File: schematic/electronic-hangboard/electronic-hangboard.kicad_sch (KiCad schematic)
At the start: 40 parts, among them J1 UART, J2 Load cell, J3 JTAG, J4 Battery, Q1 2N7002, SW1 RESET, SW2 POWER_ON, U1 ESP32-WROOM-32, U2 HX711, U3 NCP1400A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

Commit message: Update pcb
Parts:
- removed C10: 68uF, Capacitor_SMD:C_1206_3216Metric_Pad1.33x1.80mm_HandSolder, symbol Device:C
- removed C9: 10uF, Capacitor_SMD:C_1206_3216Metric_Pad1.33x1.80mm_HandSolder, symbol Device:C
- removed D1: MBR0520LT1, Diode_SMD:D_SOD-123, symbol Device:D
- removed J1: UART, Connector_PinHeader_2.54mm:PinHeader_1x03_P2.54mm_Vertical, symbol Connector_Generic:Conn_01x03
- removed J2: Load cell, Connector_Wire:SolderWire-0.1sqmm_1x04_P3.6mm_D0.4mm_OD1mm_Relief, symbol Connector_Generic:Conn_01x04
- removed J3: JTAG, Connector_PinHeader_2.54mm:PinHeader_1x07_P2.54mm_Vertical, symbol Connector:AVR-JTAG-10
- removed J4: Battery, Connector_Wire:SolderWire-0.1sqmm_1x02_P3.6mm_D0.4mm_OD1mm, symbol Connector_Generic:Conn_01x02
- removed L1: CR54−220MC - 22uH, Inductor_SMD:L_Bourns_SRP7028A_7.3x6.6mm, symbol Device:L
- removed Q1: 2N7002, Package_TO_SOT_SMD:SOT-23, symbol Transistor_FET:2N7002
- removed R8: 100R, Resistor_SMD:R_1206_3216Metric_Pad1.30x1.75mm_HandSolder, symbol Device:R
- removed SW1: RESET, Button_Switch_SMD:SW_Push_1P1T_NO_6x6mm_H9.5mm, symbol Switch:SW_SPST
- removed SW2: POWER_ON, Button_Switch_SMD:SW_Push_1P1T_NO_6x6mm_H9.5mm, symbol Switch:SW_SPST
- removed U3: NCP1400A, Package_TO_SOT_SMD:SOT-23-5_HandSoldering, symbol ncp1400a:NCP1400A
- added C13, C15: 4.7uF, Capacitor_SMD:C_1206_3216Metric_Pad1.33x1.80mm_HandSolder, symbol Device:C
- added C14: 3.3pF, Capacitor_SMD:C_1206_3216Metric_Pad1.33x1.80mm_HandSolder, symbol Device:C
- added D1, D3: LED, Diode_SMD:D_1206_3216Metric_Pad1.42x1.75mm_HandSolder, symbol Device:LED
- added D2: MBR0520LT1, Diode_SMD:D_SOD-123, symbol Device:D
- added J1: BATTERY, Connector_PinHeader_2.54mm:PinHeader_1x02_P2.54mm_Vertical, symbol Connector:Conn_01x02_Pin
- added J2: Conn_01x04_Pin, Connector_PinHeader_2.54mm:PinHeader_1x04_P2.54mm_Vertical, symbol Connector:Conn_01x04_Pin
- added J3: JTAG, Connector_PinHeader_2.54mm:PinHeader_1x06_P2.54mm_Vertical, symbol Connector:Conn_01x06_Pin
- added J4, J6: Conn_01x10_Pin, Connector_PinHeader_2.54mm:PinHeader_1x10_P2.54mm_Vertical, symbol Connector:Conn_01x10_Pin
- added J5: UART, Connector_PinHeader_2.54mm:PinHeader_1x06_P2.54mm_Vertical, symbol Connector:Conn_01x06_Pin
- added L2: 10uH, Inductor_SMD:L_Bourns_SRP7028A_7.3x6.6mm, symbol Device:L
- added Q1: S9015, Package_TO_SOT_SMD:SOT-23, symbol Simulation_SPICE:PNP
- added R1: 620K, Resistor_SMD:R_1206_3216Metric_Pad1.30x1.75mm_HandSolder, symbol Device:R
- added R1: 200K, Resistor_SMD:R_1206_3216Metric_Pad1.30x1.75mm_HandSolder, symbol Device:R
- added R12, R15: 330R, Resistor_SMD:R_1206_3216Metric_Pad1.30x1.75mm_HandSolder, symbol Device:R
- added SW3: POWER_ON, Connector_PinHeader_2.54mm:PinHeader_1x02_P2.54mm_Vertical_SMD_Pin1Left, symbol Switch:SW_SPST
- added U5: TPS61040DBV, Package_TO_SOT_SMD:SOT-23-5, symbol Regulator_Switching:TPS61040DBV
- H1, H2, H3: footprint MountingHole:MountingHole_3.2mm_M3 -> MountingHole:MountingHole_3.2mm_M3_DIN965_Pad_TopBottom
- R1: value R -> 10K
- R9: value 100R -> 1K2
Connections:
- net +3V3: now also J3.1 (Pin_1), J5.1 (Pin_1), Q1.3 (E)
- net +5V: now also C14.2, C15.2, D2.1 (K), R1.1
- net +BATT: now also C13.2, J1.2 (Pin_2), L2.1, SW3.2 (B), U5.5 (VIN)
- net CONV_EN: now also SW3.1 (A), U5.4 (EN)
- net EN: now also J5.4 (Pin_4)
- net GND: now also C13.1, C15.1, J1.1 (Pin_1), J2.2 (Pin_2), J3.2 (Pin_2), J5.2 (Pin_2), R1.2, R12.1, R15.2, U5.2 (GND)
- net RX: now also J5.6 (Pin_6)
- net S+: now also J2.3 (Pin_3)
- net S-: now also C7.2, U2.7 (INA-), J2.4 (Pin_4)
- net SCK: now also U1.20 (SCK/CLK), J4.4 (Pin_4); no longer U1.31 (IO19), U2.11 (PD_SCK)
- net TX: now also J5.5 (Pin_5)
- net at R2.1: now also J3.3 (Pin_3)
- net at R3.1: now also J3.4 (Pin_4)
- net at R4.1: now also J3.5 (Pin_5)
- net at R5.1: now also J3.6 (Pin_6)
- net RST: now reaches U1.25 (IO0)
- net RST: now also J5.3 (Pin_3)
- net E+: now reaches C6.2, R6.1, U2.3 (AVDD)
- net E+: now also J2.1 (Pin_1), Q1.1 (C)
- net at U2.2 (BASE): now also Q1.2 (B)
- net IO25: now reaches U1.10 (IO25)
- net IO25: now also J4.10 (Pin_10)
- net IO26: now reaches U1.11 (IO26)
- net IO26: now also J4.9 (Pin_9)
- net IO27: now reaches U1.12 (IO27)
- net IO27: now also J4.8 (Pin_8)
- net SHD: now reaches U1.17 (SHD/SD2)
- net SHD: now also J4.7 (Pin_7)
- net SWP: now reaches U1.18 (SWP/SD3)
- net SWP: now also J4.6 (Pin_6)
- net SCS: now reaches U1.19 (SCS/CMD)
- net SCS: now also J4.5 (Pin_5)
- net SDO: now reaches U1.21 (SDO/SD0)
- net SDO: now also J4.3 (Pin_3)
- net SDI: now reaches U1.22 (SDI/SD1)
- net SDI: now also J4.2 (Pin_2)
- net IO2: now reaches U1.24 (IO2)
- net IO2: now also J4.1 (Pin_1)
- net IO21: now reaches U1.33 (IO21)
- net IO21: now also J6.7 (Pin_7)
- net IO22: now reaches U1.36 (IO22)
- net IO22: now also D3.2 (A), J6.8 (Pin_8)
- net IO23: now reaches U1.37 (IO23)
- net IO23: now also D1.2 (A), J6.9 (Pin_9)
- net VP: now reaches U1.4 (SENSOR_VP)
- net VP: now also J6.6 (Pin_6)
- net VN: now reaches U1.5 (SENSOR_VN)
- net VN: now also J6.5 (Pin_5)
- net IO34: now reaches U1.6 (IO34)
- net IO34: now also J6.4 (Pin_4)
- net IO35: now reaches U1.7 (IO35)
- net IO35: now also J6.3 (Pin_3)
- net IO32: now reaches U1.8 (IO32)
- net IO32: now also J6.2 (Pin_2)
- net IO33: now reaches U1.9 (IO33)
- net IO33: now also J6.1 (Pin_1)
- new net: C14.1, R1.1, R1.2, U5.3 (FB)
- new net: D3.1 (K), R15.1
- new net: D1.1 (K), R12.2
- new net: D2.2 (A), L2.2, U5.1 (SW)
- new net HX711_SCK: U1.31 (IO19), U2.11 (PD_SCK)
- no-connect marks 21 -> 1
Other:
- moved on the sheet: R2, R3, R4, R5

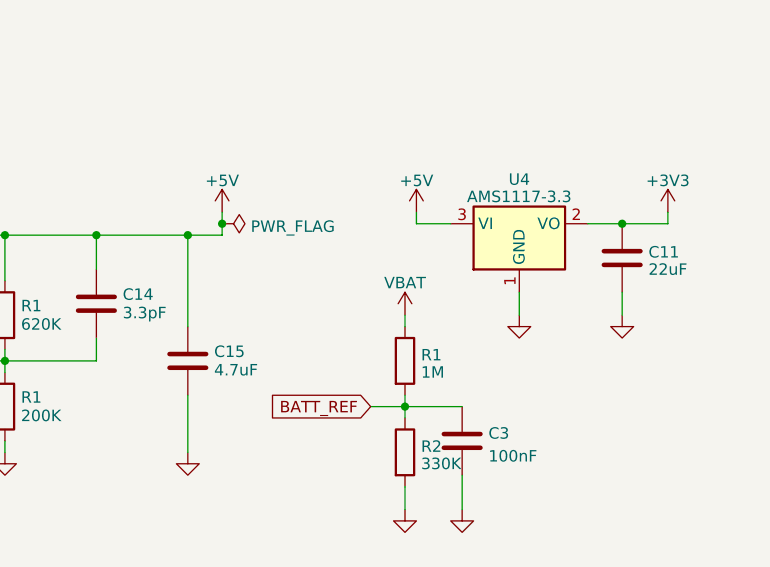
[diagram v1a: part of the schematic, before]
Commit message: update schematic fix voltage divider not connected
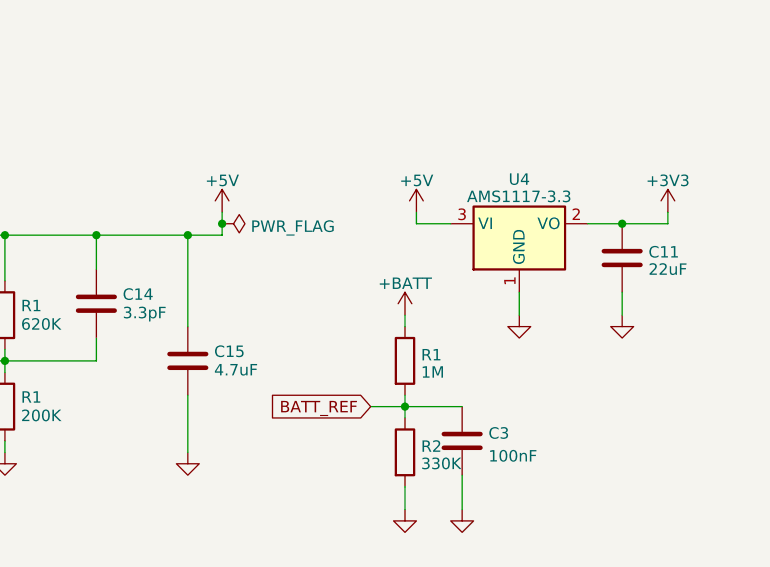
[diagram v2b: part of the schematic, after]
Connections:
- net VBAT is gone; now on net +BATT: R1.1
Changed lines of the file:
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@@
-    )
-  )
-  (symbol (lib_id "pkl_power:VBAT") (at 246.38 138.43 0) (unit 1)
-    (in_bom yes) (on_board yes) (dnp no) (fields_autoplaced)
-    (property "Reference" "#PWR0102" (at 246.38 142.24 0)
-      (effects (font (size 1.27 1.27)) hide)
-    )
-    (property "Value" "VBAT" (at 246.38 134.8542 0)
-      (effects (font (size 1.27 1.27)))
-    )
-    (property "Footprint" "" (at 246.38 138.43 0)
-      (effects (font (size 1.27 1.27)) hide)
-    )
-    (property "Datasheet" "" (at 246.38 138.43 0)
-      (effects (font (size 1.27 1.27)) hide)
-    )
-    (pin "1")
-    (instances
-      (project "meteo_2"
-        (path "/e9908eee-3e97-4614-a5f4-fd4f28d04543"
-          (reference "#PWR0102") (unit 1)
-        )
-      )
-      (project "electronic-hangboard"
-        (path "/ecd16e9a-0fdc-44a0-8eee-a04d668b68f5"
-          (reference "#PWR028") (unit 1)
-        )
-      )
     )
   )
@@
         )
       )
+    )
+  )
+  (symbol (lib_id "power:+BATT") (at 246.38 138.43 0) (unit 1)
+    (in_bom yes) (on_board yes) (dnp no) (fields_autoplaced)
+    (property "Reference" "#PWR019" (at 246.38 142.24 0)
+      (effects (font (size 1.27 1.27)) hide)
+    )
+    (property "Value" "+BATT" (at 246.38 134.9281 0)
+      (effects (font (size 1.27 1.27)))
+    )
+    (property "Footprint" "" (at 246.38 138.43 0)
+      (effects (font (size 1.27 1.27)) hide)
+    )
+    (property "Datasheet" "" (at 246.38 138.43 0)
+      (effects (font (size 1.27 1.27)) hide)
+    )
+    (pin "1")
+    (instances
+      (project "electronic-hangboard"
+        (path "/ecd16e9a-0fdc-44a0-8eee-a04d668b68f5"
+          (reference "#PWR019") (unit 1)
+        )
+      )
